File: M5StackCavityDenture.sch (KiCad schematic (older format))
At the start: 15 parts, among them J1 Conn_01x04, J2 Conn_01x08, J3 free_holes, J4 Conn_01x08, J5 Conn_01x02, U1 SP3485EN

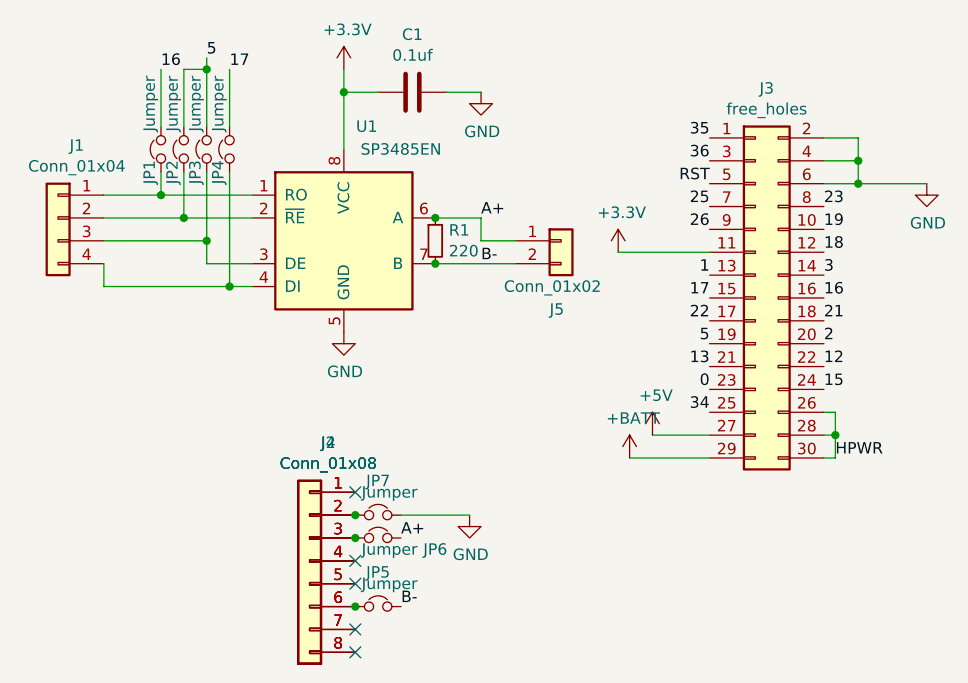
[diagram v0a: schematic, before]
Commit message: Remove redundant components
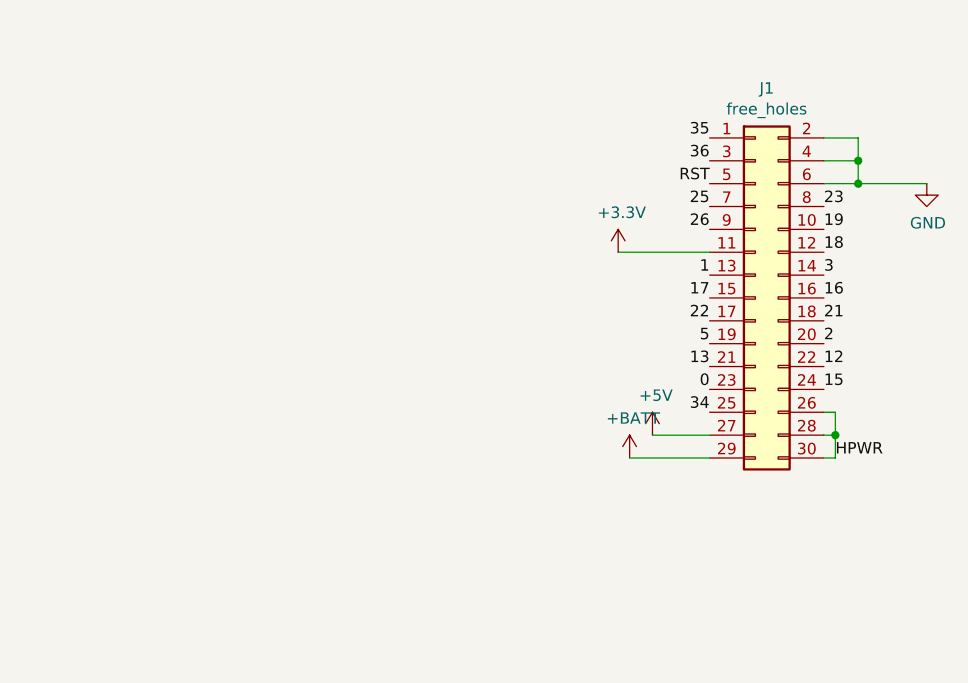
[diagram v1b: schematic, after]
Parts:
- removed C1: 0.1uf, Capacitor_SMD:C_0603_1608Metric, symbol Device:C
- removed J1: Conn_01x04, Connector_PinHeader_1.27mm:PinHeader_1x04_P1.27mm_Vertical, symbol Connector_Generic:Conn_01x04
- removed J2: Conn_01x08, Connector_PinHeader_1.27mm:PinHeader_1x08_P1.27mm_Vertical, symbol Connector_Generic:Conn_01x08
- removed J4: Conn_01x08, footprints:RJ45_Neltron_Industrial_7810-8P8C, symbol Connector_Generic:Conn_01x08
- removed J5: Conn_01x02, Connector_PinHeader_1.27mm:PinHeader_1x02_P1.27mm_Vertical, symbol Connector_Generic:Conn_01x02
- removed JP1, JP2, JP3, JP4, JP5, JP6, JP7: Jumper, Jumper:SolderJumper-2_P1.3mm_Bridged_RoundedPad1.0x1.5mm, symbol Device:Jumper_NC_Small
- removed R1: 220, Resistor_SMD:R_0603_1608Metric, symbol Device:R_Small
- removed U1: SP3485EN, Package_SO:SOIC-8_3.9x4.9mm_P1.27mm, symbol Interface_UART:SP3485EN
- renumbered J3 to J1
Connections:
- no-connect marks 5 -> 0
